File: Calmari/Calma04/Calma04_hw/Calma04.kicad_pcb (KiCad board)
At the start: 2 copper layers, 57 x 12 mm, 31 parts, among them Q1 ALS, Q2 LED_RGB 5050, SW1 SWITCH

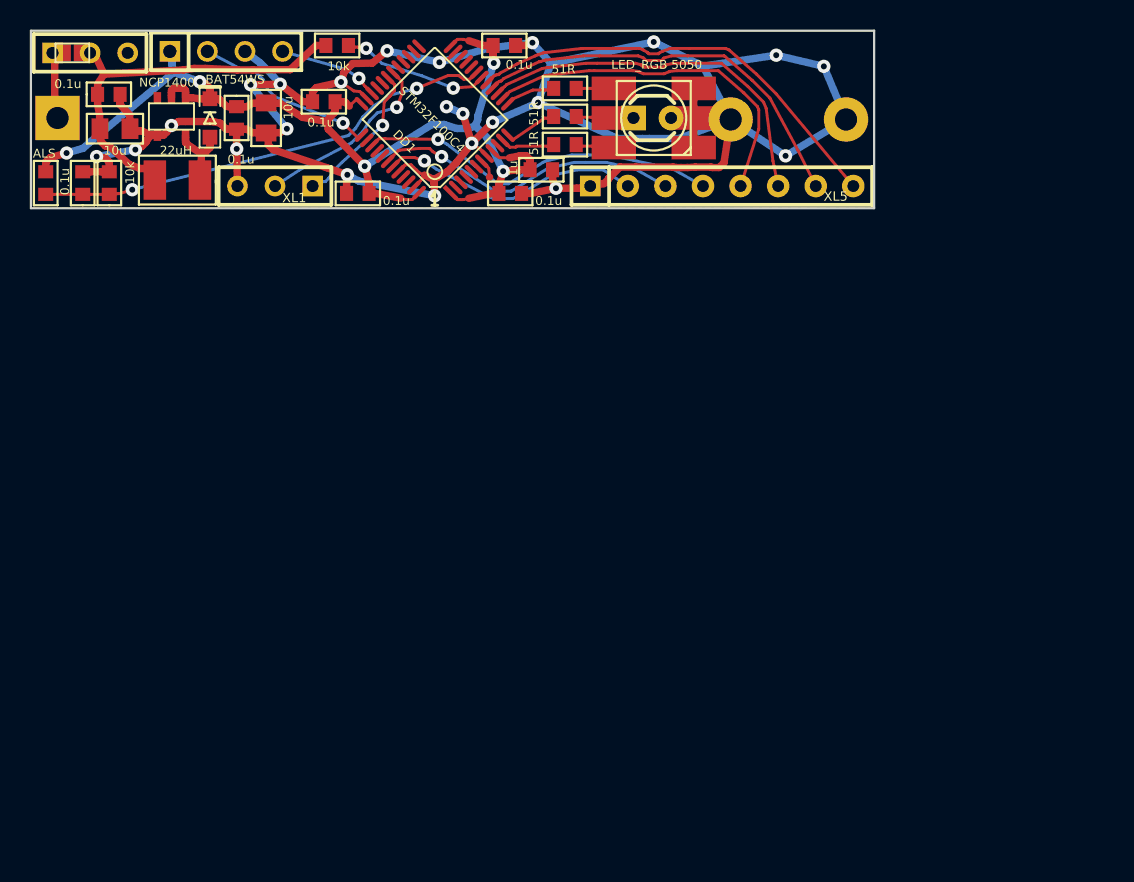
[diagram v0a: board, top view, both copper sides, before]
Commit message: calma04 pcb added
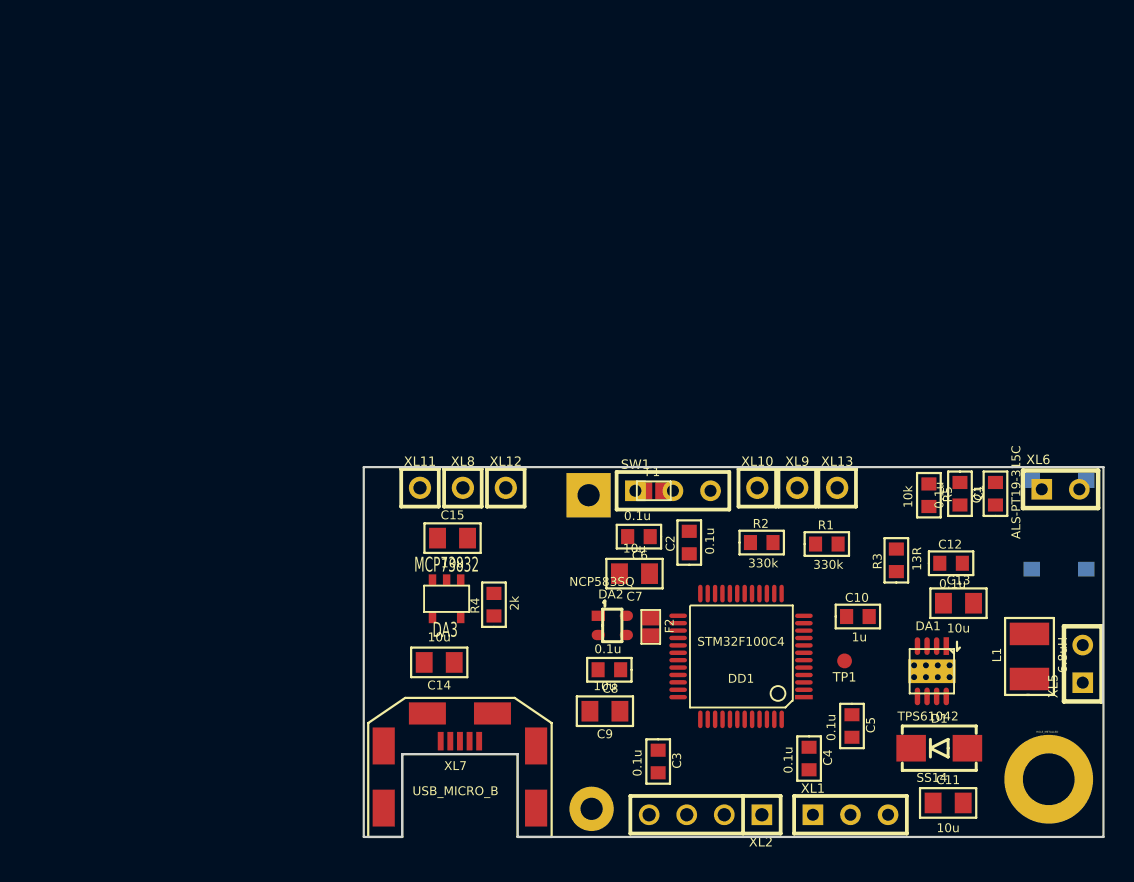
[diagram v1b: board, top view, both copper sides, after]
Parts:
- removed D2: LED, LED-3MM
- removed Q2: LED_RGB 5050, LED_HH5050_RGB
- added C11: 10u, CAP_0805, F.Cu at (157.0, 147.2)
- added C12: 0.1u, CAP_0603, F.Cu at (157.2, 131.0)
- added C13: 10u, CAP_0805, F.Cu at (157.7, 133.7)
- added C14: 10u, CAP_0805, F.Cu at (122.6, 137.7)
- added C15: 10u, CAP_0805, F.Cu at (123.5, 129.3)
- added DA2: NCP583SQ, SC82AB, F.Cu at (134.3, 135.2)
- added DA3: MCP73832, SOT23-5, F.Cu at (123.1, 133.4)
- added F2: FUSE0R, SMD0603_FUSE, F.Cu at (136.9, 135.3)
- added HOLE2: HOLE_METALLED, Hole3_5_out6mm, F.Cu at (163.8, 145.6)
- added SW2: BUTTON, BUTTON_4x4_SMD, B.Cu at (164.5, 128.4)
- added XL10: CONN_1, SIL-1, F.Cu at (144.1, 125.9)
- added XL11: CONN_1, SIL-1, F.Cu at (121.3, 125.9)
- added XL12: CONN_1, SIL-1, F.Cu at (127.1, 125.9)
- added XL13: CONN_1, SIL-1, F.Cu at (149.5, 125.9)
- added XL7: USB_MICRO_B, USBmicro_MOLEX_WM17142, F.Cu at (124.0, 143.9)
- added XL8: CONN_1, SIL-1, F.Cu at (124.2, 125.9)
- added XL9: CONN_1, SIL-1, F.Cu at (146.8, 125.9)
- D1: value BAT54WS -> SS14; footprint DIODE_SOD323 -> DIODE_SMA_DO214AC
- DA1: value NCP1400 -> TPS61042; footprint SOT23-5 -> DRB8
- L1: value 22uH -> 6.8uH
- Q1: value ALS -> ALS-PT19-315C
- R1: value 51R -> 330k
- R2: value 10k -> 330k
- R3: value 51R -> 13R
- R4: value 51R -> 2k
- TP1: footprint TESTPOINT_0_5MM -> TESTPOINT_1MM
- XL5: value CONN_8 -> CONN_2; footprint SIL-8 -> SIL-2
- XL6: value CONN_1 -> CONN_2; footprint SIL1_ROUND_1MM5 -> SIL-2
- moved Q1 67.5 mm to (160.2, 126.3), turned to 90 degrees
- moved L1 66.0 mm to (162.5, 137.3), turned to 90 degrees
- moved D1 65.2 mm to (156.4, 143.5), turned to 0 degrees
- moved DA1 63.6 mm to (155.9, 138.3)
- moved C1 62.9 mm to (157.8, 126.3), turned to 270 degrees
- moved XL2 60.9 mm to (140.6, 148.0), turned to 180 degrees
- moved R5 59.3 mm to (155.7, 126.4), turned to 270 degrees
- moved XL1 57.6 mm to (150.4, 148.0), turned to 0 degrees
- moved C3 50.0 mm to (137.4, 144.4), turned to 270 degrees
- moved XL4 49.7 mm to (132.9, 147.6)
- moved SW1 49.3 mm to (138.4, 126.1)
- moved F1 49.2 mm to (137.1, 126.1)
- moved C4 48.9 mm to (147.6, 144.2), turned to 270 degrees
- moved C6 46.7 mm to (136.1, 129.2), turned to 180 degrees
- moved C7 46.2 mm to (135.8, 131.7), turned to 180 degrees
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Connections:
- D1 pad A: /Lout -> N-0000024
- D1 pad C: +3.3V -> N-0000022
- DA1 pad 1: +3.3V -> N-0000021
- DA1 pad 2: +3.3V -> N-0000025
- DA1 pad 3: (no net) -> +BATT
- DA1 pad 4: GND -> N-0000025
- DA1 pad 5: /Lout -> N-0000027
- DD1 pad 10: (no net) -> /BTN
- DD1 pad 11: N-0000028 -> N-0000027
- DD1 pad 12: N-0000027 -> (no net)
- DD1 pad 13: N-0000020 -> (no net)
- DD1 pad 14: /5 -> (no net)
- DD1 pad 15: /6 -> (no net)
- DD1 pad 16: /7 -> (no net)
- DD1 pad 17: /8 -> /Charge
- DD1 pad 18: N-000004 (its old number) -> N-000005
- DD1 pad 39: /4 -> (no net)
- DD1 pad 42: /3 -> (no net)
- DD1 pad 43: /2 -> (no net)
- L1 pad 1: /Lout -> N-0000024
- R1 pad 1: N-0000027 -> N-000005
- R1 pad 2: N-0000029 -> GND
- R2 pad 2: N-000004 (its old number) -> N-000005
- R3 pad 1: N-0000020 -> N-0000025
- R3 pad 2: N-0000030 -> GND
- R4 pad 1: N-0000028 -> N-0000019
- R4 pad 2: N-000008 -> GND
- XL5 pad 1: GND -> N-0000022
- XL5 pad 2: /2 -> N-0000021
- XL6 pad 1: GND -> /BTN
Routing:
- net GND: track 173.2 -> 0.00 mm, vias 23 -> 0
- net +3.3V: track 72.9 -> 0.00 mm, vias 5 -> 0
- net N-000003: track 31.3 -> 0.00 mm, vias 2 -> 0
- net /8: track 29.6 -> 0.00 mm
- net +BATT: track 27.5 -> 0.00 mm
- net /7: track 27.3 -> 0.00 mm
- net /6: track 25.4 -> 0.00 mm
- net /4: track 24.5 -> 0.00 mm, vias 1 -> 0
- net /5: track 24.3 -> 0.00 mm
- net /3: track 20.8 -> 0.00 mm, vias 1 -> 0
- net /2: track 17.6 -> 0.00 mm, vias 1 -> 0
- net /TX: track 12.7 -> 0.00 mm, vias 1 -> 0
- net /SB_SWCLK: track 12.4 -> 0.00 mm, vias 1 -> 0
- net /RX: track 10.1 -> 0.00 mm, vias 1 -> 0
- net N-000004 (its old number): track 9.99 -> 0.00 mm, vias 2 -> 0
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- removed copper zone on B.Cu, net GND
- removed copper zone on F.Cu, net GND
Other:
- board size 57 x 12 mm -> 50 x 25 mm
- net class Default: clearance 0.2 -> 0.254; trace_width 0.2 -> 0.254; via_dia 0.9 -> 0.889; via_drill 0.4 -> 0.635
- net class Wide removed
- rule pad_to_mask_clearance: 0.1 -> 0.2
- rule trace_clearance: 0.2 -> 0.254
- rule trace_min: 0.2 -> 0.254
- rule via_min_drill: 0.4 -> 0.508

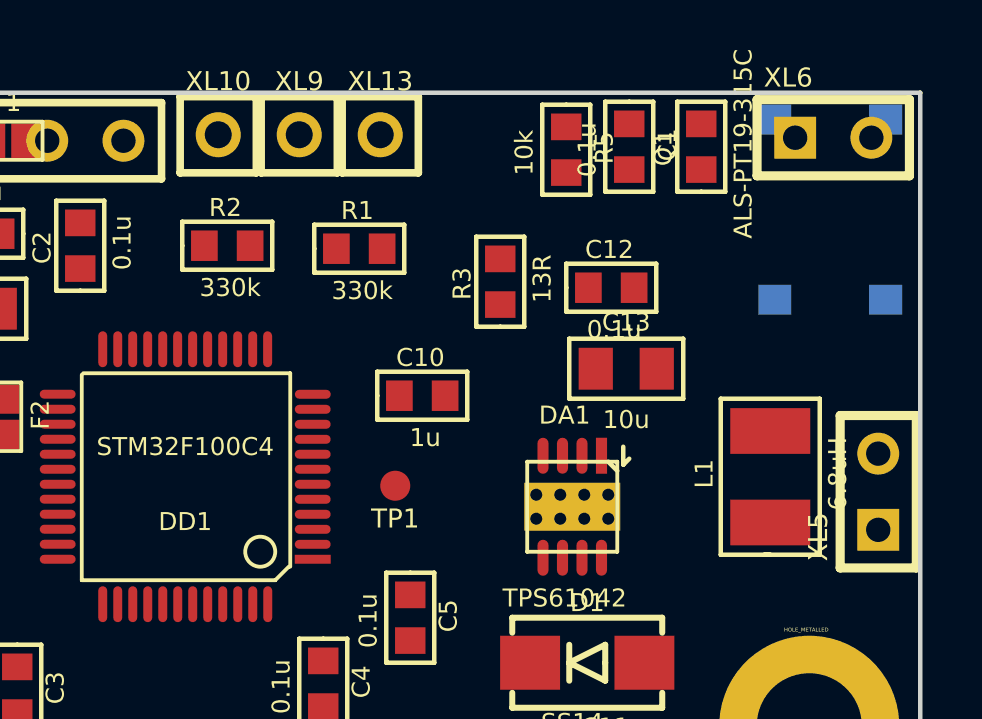
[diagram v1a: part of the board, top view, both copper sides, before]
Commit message: 
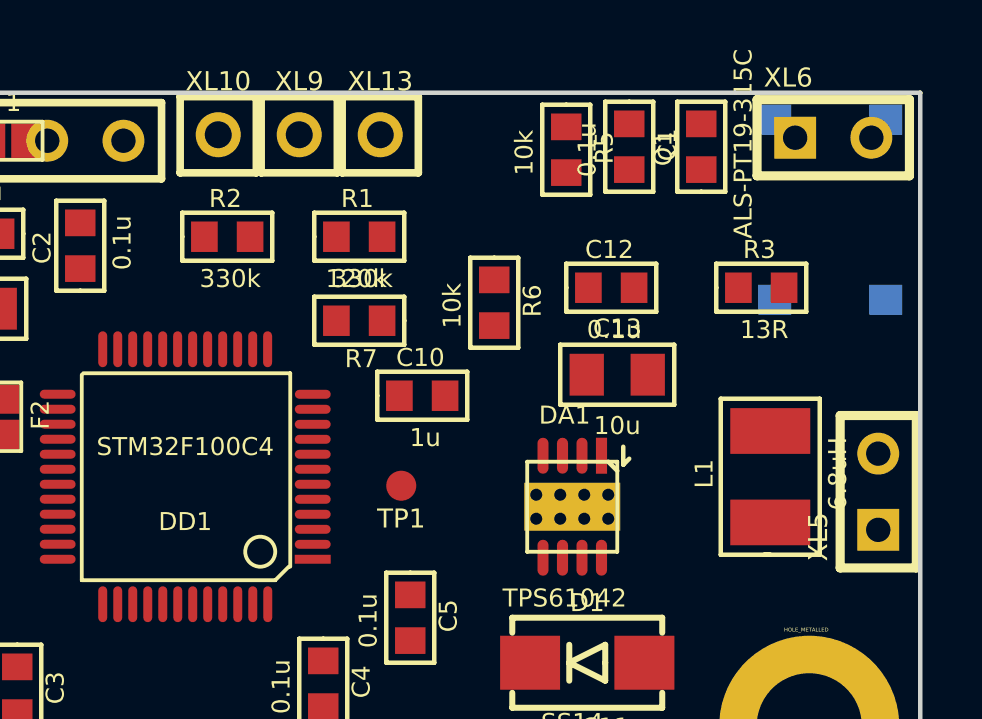
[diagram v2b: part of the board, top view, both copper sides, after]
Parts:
- added R6: 10k, RES_0603, F.Cu at (153.3, 131.5)
- added R7: 120k, RES_0603, F.Cu at (148.8, 132.1)
- moved R3 8.70 mm to (162.2, 131.0), turned to 0 degrees
- moved R1 0.40 mm to (148.8, 129.3)
- moved C13 0.36 mm to (157.4, 133.9)
- moved R2 0.30 mm to (144.4, 129.3)
- moved TP1 0.20 mm to (150.2, 137.6)
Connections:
- DA1 pad 2: N-0000025 -> N-0000018
- DA1 pad 4: N-0000025 -> N-0000017
- DD1 pad 14: (no net) -> /FB
- R3 pad 1: N-0000025 -> N-0000018

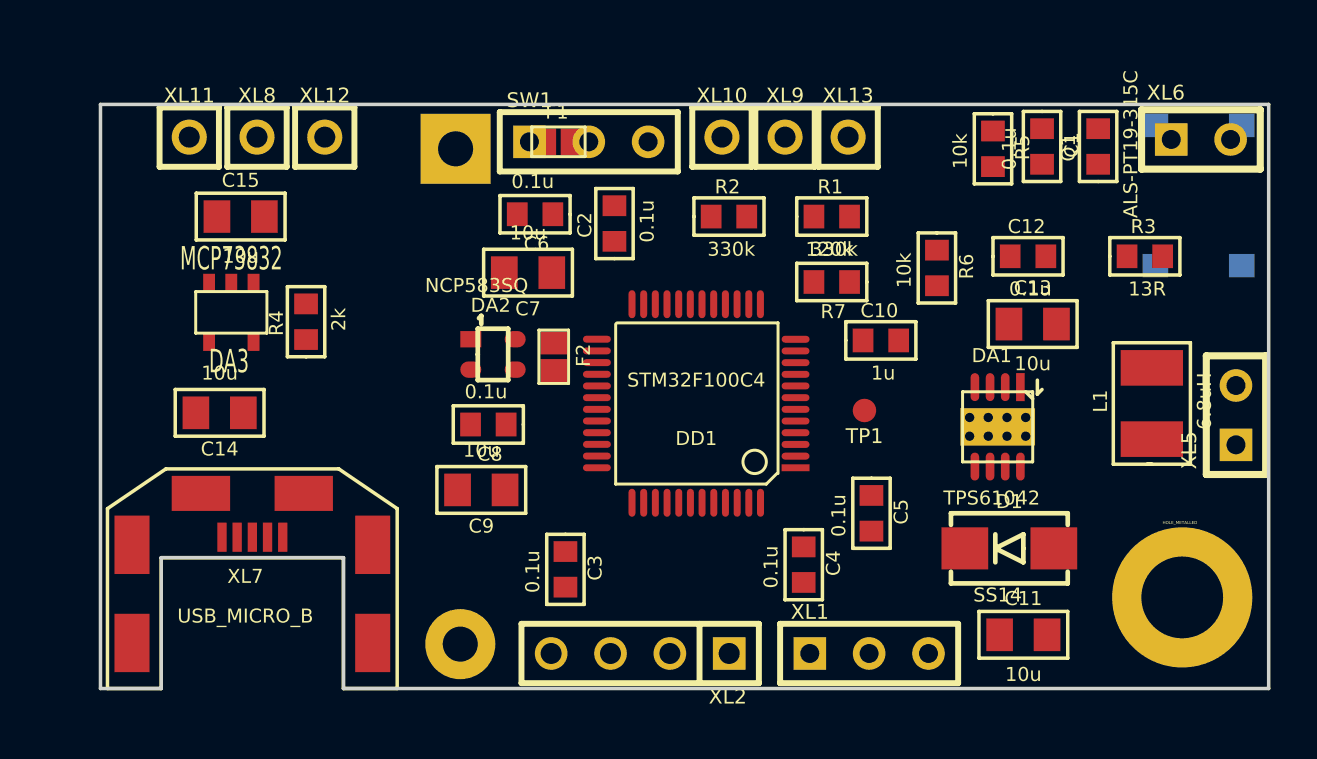
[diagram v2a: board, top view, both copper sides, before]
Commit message: 
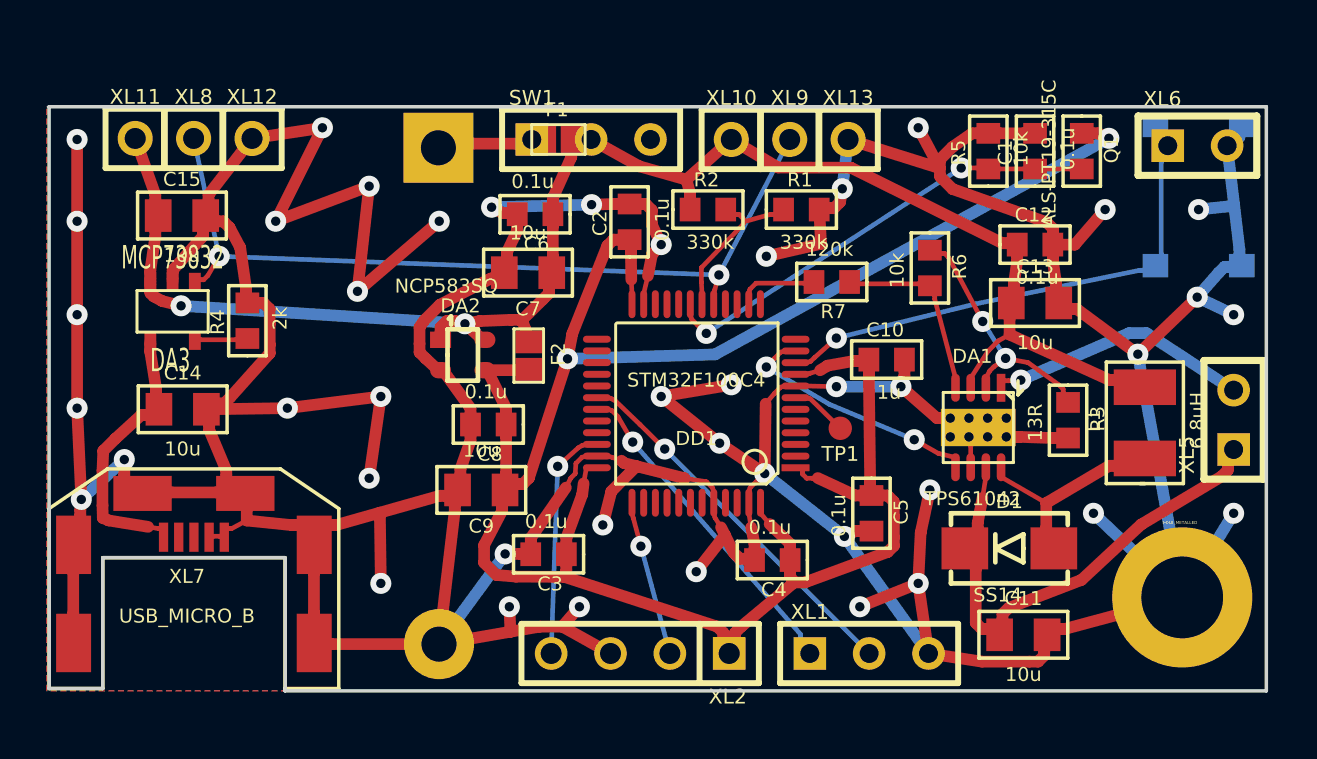
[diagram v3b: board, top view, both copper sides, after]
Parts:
- moved R3 7.75 mm to (158.9, 138.0), turned to 270 degrees
- moved XL12 3.11 mm to (124.0, 126.0)
- moved XL8 2.71 mm to (121.5, 126.0)
- moved C15 2.51 mm to (121.0, 129.3)
- moved R4 2.51 mm to (123.8, 133.8)
- moved DA3 2.51 mm to (120.6, 133.4)
- moved XL7 2.50 mm to (121.5, 143.9)
- moved XL11 2.31 mm to (119.0, 126.0)
- moved C14 1.59 mm to (121.0, 137.5), turned to 0 degrees
- moved C4 1.36 mm to (146.3, 144.0), turned to 180 degrees
- moved R1 1.33 mm to (147.5, 129.0)
- moved DA2 1.29 mm to (133.0, 135.2)
- moved TP1 1.29 mm to (149.2, 138.4)
- moved F2 1.07 mm to (135.8, 135.3)
- moved C3 0.97 mm to (136.7, 143.8), turned to 180 degrees
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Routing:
- net GND: track 0.00 -> 313.6 mm, vias 0 -> 43
- net +3.3V: track 0.00 -> 98.6 mm, vias 0 -> 2
- net +BATT: track 0.00 -> 70.7 mm, vias 0 -> 2
- net /Charge: track 0.00 -> 36.0 mm, vias 0 -> 2
- net N-0000022: track 0.00 -> 21.7 mm
- net /BTN: track 0.00 -> 21.4 mm, vias 0 -> 1
- net N-000003: track 0.00 -> 19.7 mm, vias 0 -> 2
- net /TX: track 0.00 -> 16.1 mm, vias 0 -> 1
- net /RX: track 0.00 -> 14.1 mm, vias 0 -> 1
- net +5V: track 0.00 -> 11.8 mm
- net N-0000021: track 0.00 -> 11.3 mm, vias 0 -> 1
- net N-0000018: track 0.00 -> 11.0 mm, vias 0 -> 2
- net N-0000020: track 0.00 -> 11.0 mm, vias 0 -> 2
- net /SB_SWDAT: track 0.00 -> 10.0 mm, vias 0 -> 1
- net N-0000024: track 0.00 -> 9.36 mm
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- added copper zone on B.Cu, net GND
- added copper zone on F.Cu, net GND
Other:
- board size 50 x 25 mm -> 52.1 x 25 mm
- net class Default: clearance 0.254 -> 0.2; trace_width 0.254 -> 0.2; via_dia 0.889 -> 0.9; via_drill 0.635 -> 0.4
- net class Wide added: clearance 0.2, trace_width 0.5, via_dia 0.9, via_drill 0.4
- rule pad_to_mask_clearance: 0.2 -> 0.1
- rule trace_clearance: 0.254 -> 0.2
- rule trace_min: 0.254 -> 0.2
- rule via_min_drill: 0.508 -> 0.3
- rule via_min_size: 0.889 -> 0.8
